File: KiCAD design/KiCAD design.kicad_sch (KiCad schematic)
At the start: 1 part, among them U101 NUCLEO64-F411RE

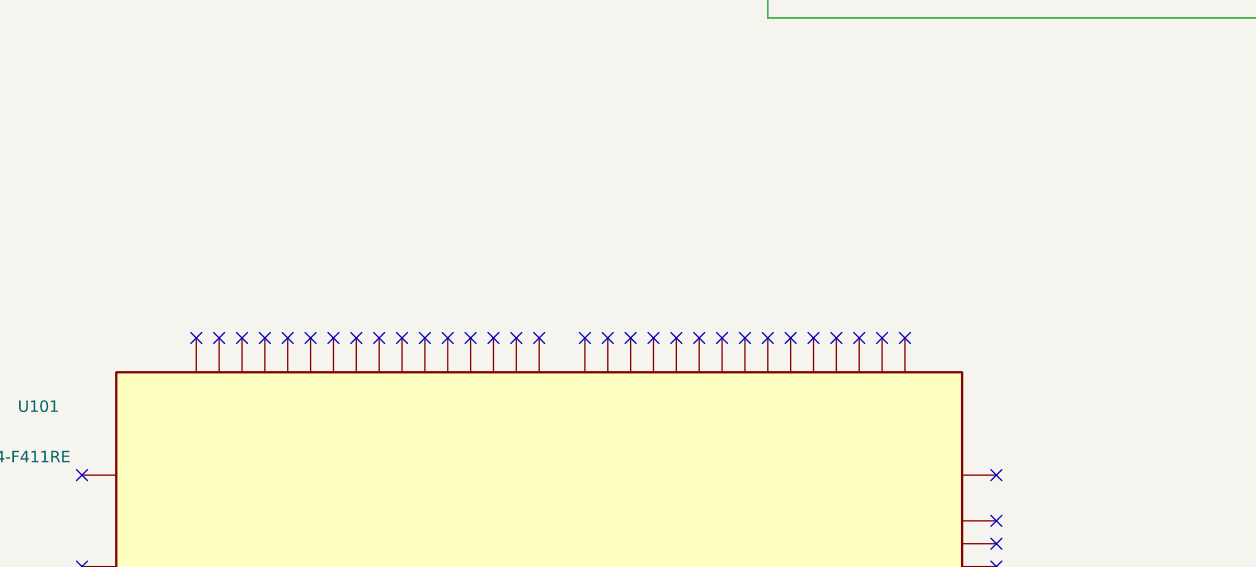
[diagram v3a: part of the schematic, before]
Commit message: comment about nucleo board in main sheet
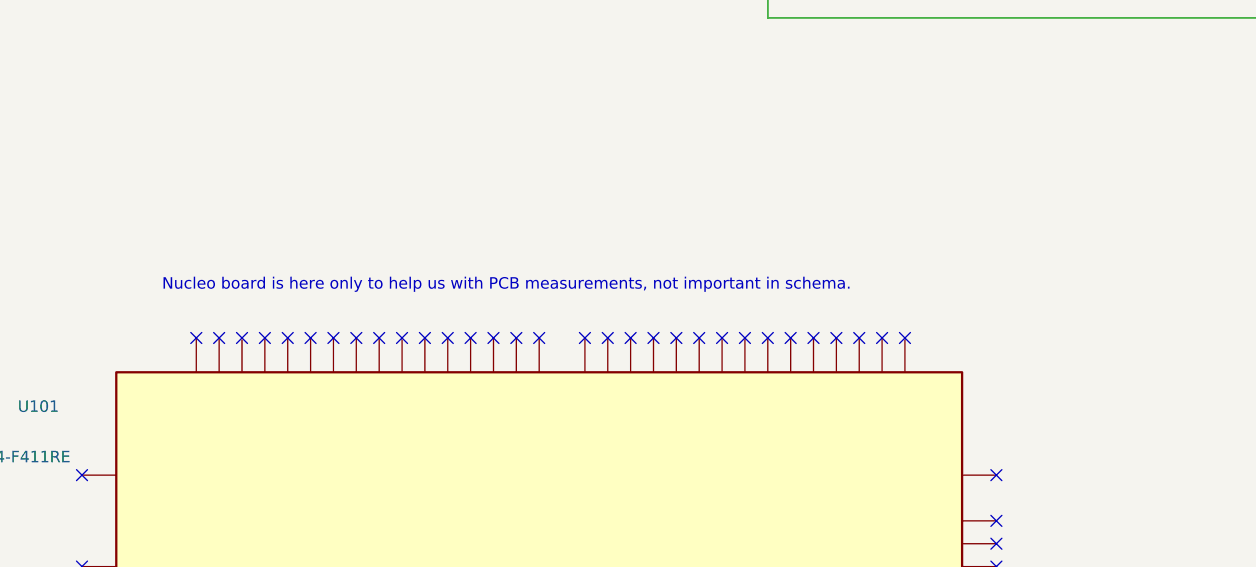
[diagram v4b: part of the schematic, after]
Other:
- note added: "Nucleo board is here only to help us with PCB measurements, not important in schema."
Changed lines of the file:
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@@
     (stroke (width 0) (type default) (color 0 0 0 0))
+  )
+  (text "Nucleo board is here only to help us with PCB measurements, not important in schema."
+    (at 52.07 116.84 0)
+    (effects (font (size 1.27 1.27)) (justify left bottom))
   )
   (symbol (lib_id "MCU_Module:NUCLEO64-F411RE") (at 93.98 149.86 90) (unit 1)

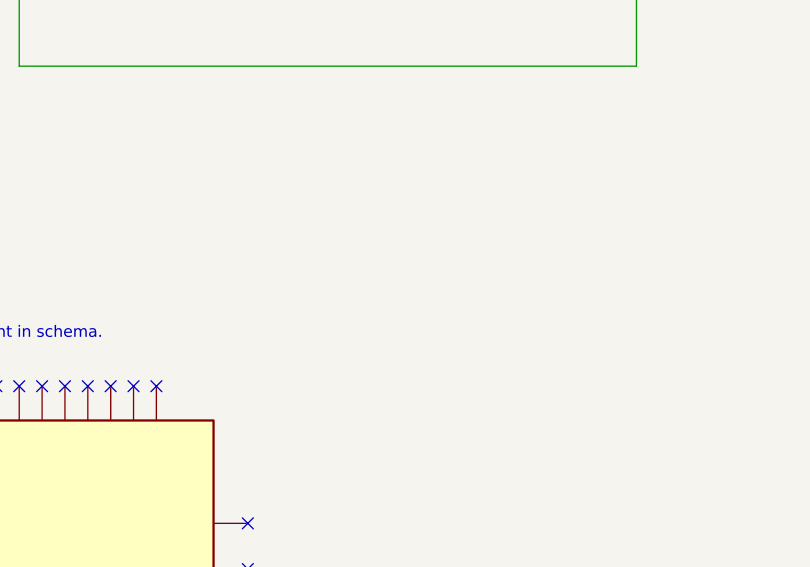
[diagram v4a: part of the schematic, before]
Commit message: change in nucleo pin
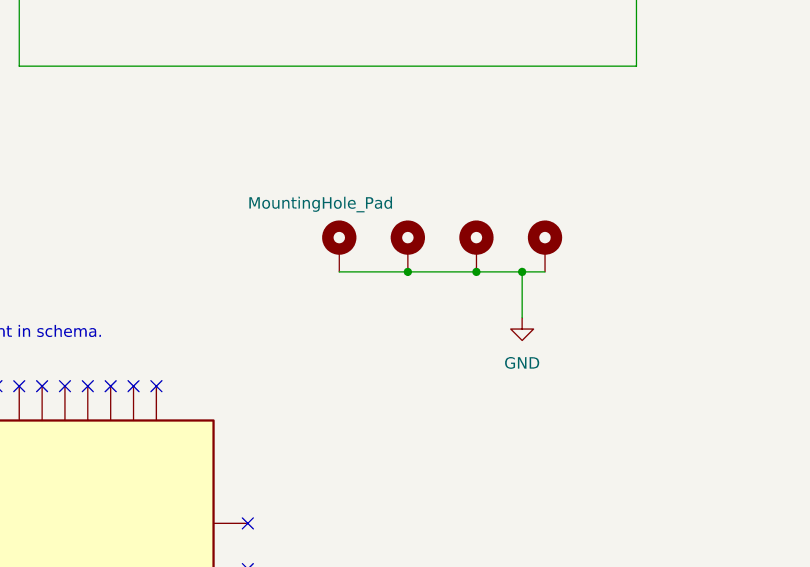
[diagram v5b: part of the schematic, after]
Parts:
- added H101, H102, H103, H104: MountingHole_Pad, MountingHole:MountingHole_3.2mm_M3_Pad_Via, symbol Mechanical:MountingHole_Pad
- U101: footprint Module:ST_Morpho_Connector_144_STLink -> NUCLEO.lib:ST_NUCLEO-F401RE
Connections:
- new net GND: H101.1, H102.1, H103.1, H104.1
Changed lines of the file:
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@@
 (kicad_sch (version 20211123) (generator eeschema)
   (paper "A4")
+  (junction (at 170.18 109.22) (diameter 0) (color 0 0 0 0)
+  )
+  (junction (at 162.56 109.22) (diameter 0) (color 0 0 0 0)
+  )
+  (junction (at 175.26 109.22) (diameter 0) (color 0 0 0 0)
+  )
   (no_connect (at 73.66 121.92))
   (no_connect (at 119.38 121.92))
@@
     (stroke (width 0) (type default) (color 0 0 0 0))
   )
+  (wire (pts (xy 175.26 109.22) (xy 175.26 114.3))
+    (stroke (width 0) (type default) (color 0 0 0 0))
+  )
+  (wire (pts (xy 175.26 109.22) (xy 177.8 109.22))
+    (stroke (width 0) (type default) (color 0 0 0 0))
+  )
+  (wire (pts (xy 154.94 109.22) (xy 162.56 109.22))
+    (stroke (width 0) (type default) (color 0 0 0 0))
+  )
   (wire (pts (xy 73.66 55.88) (xy 127 55.88))
     (stroke (width 0) (type default) (color 0 0 0 0))
@@
     (stroke (width 0) (type default) (color 0 0 0 0))
   )
+  (wire (pts (xy 162.56 109.22) (xy 170.18 109.22))
+    (stroke (width 0) (type default) (color 0 0 0 0))
+  )
   (wire (pts (xy 187.96 68.58) (xy 208.28 68.58))
     (stroke (width 0) (type default) (color 0 0 0 0))
@@
   )
   (wire (pts (xy 73.66 68.58) (xy 119.38 68.58))
+    (stroke (width 0) (type default) (color 0 0 0 0))
+  )
+  (wire (pts (xy 170.18 109.22) (xy 175.26 109.22))
     (stroke (width 0) (type default) (color 0 0 0 0))
   )
@@
     (effects (font (size 1.27 1.27)) (justify left bottom))
   )
+  (symbol (lib_id "Mechanical:MountingHole_Pad") (at 177.8 106.68 0) (unit 1)
+    (in_bom yes) (on_board yes)
+    (property "Reference" "H104" (id 0) (at 167.64 99.06 0)
+      (effects (font (size 1.27 1.27)) (justify left) hide)
+    )
+    (property "Value" "MountingHole_Pad" (id 1) (at 167.64 101.6 0)
+      (effects (font (size 1.27 1.27)) (justify left) hide)
+    )
+    (property "Footprint" "MountingHole:MountingHole_3.2mm_M3_Pad_Via" (id 2) (at 177.8 106.68 0)
+      (effects (font (size 1.27 1.27)) hide)
+    )
+    (property "Datasheet" "~" (id 3) (at 177.8 106.68 0)
+      (effects (font (size 1.27 1.27)) hide)
+    )
+    (pin "1")
+  )
+  (symbol (lib_id "Mechanical:MountingHole_Pad") (at 154.94 106.68 0) (unit 1)
+    (in_bom yes) (on_board yes)
+    (property "Reference" "H101" (id 0) (at 144.78 99.06 0)
+      (effects (font (size 1.27 1.27)) (justify left) hide)
+    )
+    (property "Value" "MountingHole_Pad" (id 1) (at 144.78 101.6 0)
+      (effects (font (size 1.27 1.27)) (justify left))
+    )
+    (property "Footprint" "MountingHole:MountingHole_3.2mm_M3_Pad_Via" (id 2) (at 154.94 106.68 0)
+      (effects (font (size 1.27 1.27)) hide)
+    )
+    (property "Datasheet" "~" (id 3) (at 154.94 106.68 0)
+      (effects (font (size 1.27 1.27)) hide)
+    )
+    (pin "1")
+  )
   (symbol (lib_id "MCU_Module:NUCLEO64-F411RE") (at 93.98 149.86 90) (unit 1)
-    (in_bom no) (on_board yes)
+    (in_bom no) (on_board no)
     (property "Reference" "U101" (id 0) (at 40.64 129.54 90)
       (effects (font (size 1.27 1.27)) (justify left))
@@
       (effects (font (size 1.27 1.27)) (justify left))
     )
-    (property "Footprint" "Module:ST_Morpho_Connector_144_STLink" (id 2) (at 44.45 135.1406 0)
+    (property "Footprint" "NUCLEO.lib:ST_NUCLEO-F401RE" (id 2) (at 44.45 135.1406 0)
       (effects (font (size 1.27 1.27)) (justify left) hide)
     )
@@
     (pin "9")
   )
+  (symbol (lib_id "Mechanical:MountingHole_Pad") (at 162.56 106.68 0) (unit 1)
+    (in_bom yes) (on_board yes)
+    (property "Reference" "H102" (id 0) (at 152.4 99.06 0)
+      (effects (font (size 1.27 1.27)) (justify left) hide)
+    )
+    (property "Value" "MountingHole_Pad" (id 1) (at 152.4 101.6 0)
+      (effects (font (size 1.27 1.27)) (justify left) hide)
+    )
+    (property "Footprint" "MountingHole:MountingHole_3.2mm_M3_Pad_Via" (id 2) (at 162.56 106.68 0)
+      (effects (font (size 1.27 1.27)) hide)
+    )
+    (property "Datasheet" "~" (id 3) (at 162.56 106.68 0)
+      (effects (font (size 1.27 1.27)) hide)
+    )
+    (pin "1")
+  )
+  (symbol (lib_id "Mechanical:MountingHole_Pad") (at 170.18 106.68 0) (unit 1)
+    (in_bom yes) (on_board yes)
+    (property "Reference" "H103" (id 0) (at 160.02 99.06 0)
+      (effects (font (size 1.27 1.27)) (justify left) hide)
+    )
+    (property "Value" "MountingHole_Pad" (id 1) (at 160.02 101.6 0)
+      (effects (font (size 1.27 1.27)) (justify left) hide)
+    )
+    (property "Footprint" "MountingHole:MountingHole_3.2mm_M3_Pad_Via" (id 2) (at 170.18 106.68 0)
+      (effects (font (size 1.27 1.27)) hide)
+    )
+    (property "Datasheet" "~" (id 3) (at 170.18 106.68 0)
+      (effects (font (size 1.27 1.27)) hide)
+    )
+    (pin "1")
+  )
+  (symbol (lib_id "power:GND") (at 175.26 114.3 0) (unit 1)
+    (in_bom yes) (on_board yes) (fields_autoplaced)
+    (property "Reference" "#PWR0115" (id 0) (at 175.26 120.65 0)
+      (effects (font (size 1.27 1.27)) hide)
+    )
+    (property "Value" "GND" (id 1) (at 175.26 119.38 0))
+    (property "Footprint" "" (id 2) (at 175.26 114.3 0)
+      (effects (font (size 1.27 1.27)) hide)
+    )
+    (property "Datasheet" "" (id 3) (at 175.26 114.3 0)
+      (effects (font (size 1.27 1.27)) hide)
+    )
+    (pin "1")
+  )
   (sheet (at 127 25.4) (size 50.8 50.8) (fields_autoplaced)
     (stroke (width 0.1524) (type solid) (color 0 0 0 0))
@@
       (reference "#PWR0114") (unit 1) (value "+3.3V") (footprint "")
     )
+    (path "/90dbed91-b579-480f-b438-dea81ab13820"
+      (reference "#PWR0115") (unit 1) (value "GND") (footprint "")
+    )
     (path "/351b992e-9d0c-41fd-a6c4-f130ac0d9617/ee57b0d0-fc53-46a4-955b-95d218665177"
       (reference "#PWR0201") (unit 1) (value "GND") (footprint "")
@@
       (reference "D403") (unit 1) (value "RED") (footprint "LED_SMD:LED_1206_3216Metric")
     )
+    (path "/359b6eae-d01f-4c07-a65f-0210ec982c6a"
+      (reference "H101") (unit 1) (value "MountingHole_Pad") (footprint "MountingHole:MountingHole_3.2mm_M3_Pad_Via")
+    )
+    (path "/5c3fe545-b369-450e-a10b-a0b610268b87"
+      (reference "H102") (unit 1) (value "MountingHole_Pad") (footprint "MountingHole:MountingHole_3.2mm_M3_Pad_Via")
+    )
+    (path "/882c6f9a-d699-4f16-be4b-a2264fdad17d"
+      (reference "H103") (unit 1) (value "MountingHole_Pad") (footprint "MountingHole:MountingHole_3.2mm_M3_Pad_Via")
+    )
+    (path "/1327a356-e8db-4ffb-895c-129e588e195c"
+      (reference "H104") (unit 1) (value "MountingHole_Pad") (footprint "MountingHole:MountingHole_3.2mm_M3_Pad_Via")
+    )
     (path "/351b992e-9d0c-41fd-a6c4-f130ac0d9617/73cd9a15-3818-472e-a397-2c2e429393a2"
       (reference "J201") (unit 1) (value "Conn_02x19_Odd_Even") (footprint "Connector_PinHeader_2.54mm:PinHeader_2x19_P2.54mm_Vertical")
@@
     )
     (path "/465a2d22-51a7-48d6-b1e0-fc75f581e914/f474059f-5e64-4ec2-8fdf-47fcddcb3229"
-      (reference "SW301") (unit 1) (value "~") (footprint "composants_projet_footprint:1A11-NF5STSE-B")
+      (reference "SW301") (unit 1) (value "~") (footprint "SWITCH lib:E-SWITCH_RR511D1121")
     )
     (path "/84eed88b-177a-45c5-a159-b80e42fc88fa/1effef2d-bafc-46de-9853-a1755d0a3819"
@@
     )
     (path "/53ab80cb-680d-47b5-9042-b10ff93ac434"
-      (reference "U101") (unit 1) (value "NUCLEO64-F411RE") (footprint "Module:ST_Morpho_Connector_144_STLink")
+      (reference "U101") (unit 1) (value "NUCLEO64-F411RE") (footprint "NUCLEO.lib:ST_NUCLEO-F401RE")
     )
     (path "/465a2d22-51a7-48d6-b1e0-fc75f581e914/9480c12b-095c-4fc3-a989-57ee26360abb"

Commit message: exclude mounting holes from BOM
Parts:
- H101, H102, H103, H104: now left out of the parts list
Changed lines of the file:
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@@
   )
   (symbol (lib_id "Mechanical:MountingHole_Pad") (at 177.8 106.68 0) (unit 1)
-    (in_bom yes) (on_board yes)
+    (in_bom no) (on_board yes)
     (property "Reference" "H104" (id 0) (at 167.64 99.06 0)
       (effects (font (size 1.27 1.27)) (justify left) hide)
@@
   )
   (symbol (lib_id "Mechanical:MountingHole_Pad") (at 154.94 106.68 0) (unit 1)
-    (in_bom yes) (on_board yes)
+    (in_bom no) (on_board yes)
     (property "Reference" "H101" (id 0) (at 144.78 99.06 0)
       (effects (font (size 1.27 1.27)) (justify left) hide)
@@
   )
   (symbol (lib_id "Mechanical:MountingHole_Pad") (at 162.56 106.68 0) (unit 1)
-    (in_bom yes) (on_board yes)
+    (in_bom no) (on_board yes)
     (property "Reference" "H102" (id 0) (at 152.4 99.06 0)
       (effects (font (size 1.27 1.27)) (justify left) hide)
@@
   )
   (symbol (lib_id "Mechanical:MountingHole_Pad") (at 170.18 106.68 0) (unit 1)
-    (in_bom yes) (on_board yes)
+    (in_bom no) (on_board yes)
     (property "Reference" "H103" (id 0) (at 160.02 99.06 0)
       (effects (font (size 1.27 1.27)) (justify left) hide)

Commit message: end PCB
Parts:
- H101, H102, H103, H104: now in the parts list
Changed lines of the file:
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@@
   )
   (symbol (lib_id "Mechanical:MountingHole_Pad") (at 177.8 106.68 0) (unit 1)
-    (in_bom no) (on_board yes)
+    (in_bom yes) (on_board yes)
     (property "Reference" "H104" (id 0) (at 167.64 99.06 0)
       (effects (font (size 1.27 1.27)) (justify left) hide)
@@
   )
   (symbol (lib_id "Mechanical:MountingHole_Pad") (at 154.94 106.68 0) (unit 1)
-    (in_bom no) (on_board yes)
+    (in_bom yes) (on_board yes)
     (property "Reference" "H101" (id 0) (at 144.78 99.06 0)
       (effects (font (size 1.27 1.27)) (justify left) hide)
@@
   )
   (symbol (lib_id "Mechanical:MountingHole_Pad") (at 162.56 106.68 0) (unit 1)
-    (in_bom no) (on_board yes)
+    (in_bom yes) (on_board yes)
     (property "Reference" "H102" (id 0) (at 152.4 99.06 0)
       (effects (font (size 1.27 1.27)) (justify left) hide)
@@
   )
   (symbol (lib_id "Mechanical:MountingHole_Pad") (at 170.18 106.68 0) (unit 1)
-    (in_bom no) (on_board yes)
+    (in_bom yes) (on_board yes)
     (property "Reference" "H103" (id 0) (at 160.02 99.06 0)
       (effects (font (size 1.27 1.27)) (justify left) hide)
@@
       (reference "#PWR0403") (unit 1) (value "GND") (footprint "")
     )
+    (path "/351b992e-9d0c-41fd-a6c4-f130ac0d9617/0fa4013b-08dc-4836-ad16-8115d0c7be8b"
+      (reference "#PWR?") (unit 1) (value "+3.3V") (footprint "")
+    )
     (path "/84eed88b-177a-45c5-a159-b80e42fc88fa/e609e455-2f92-47cd-a338-cdee205ff5a8"
       (reference "Bluetooth401") (unit 1) (value "PMOD BLE") (footprint "")
@@
     )
     (path "/351b992e-9d0c-41fd-a6c4-f130ac0d9617/6a8b86f3-5197-4f17-9c95-637d257eaa6f"
-      (reference "J206") (unit 1) (value "JST SENS TOF") (footprint "Connector_PinHeader_2.54mm:PinHeader_1x06_P2.54mm_Vertical")
+      (reference "J206") (unit 1) (value "JST SENS TOF 2") (footprint "Connector_PinHeader_2.54mm:PinHeader_1x06_P2.54mm_Vertical")
     )
     (path "/351b992e-9d0c-41fd-a6c4-f130ac0d9617/77ef5647-5fd0-45a7-8f1c-57b486318a65"
-      (reference "J208") (unit 1) (value "JST SENS TOF") (footprint "Connector_PinHeader_2.54mm:PinHeader_1x06_P2.54mm_Vertical")
+      (reference "J208") (unit 1) (value "JST SENS TOF 1") (footprint "Connector_PinHeader_2.54mm:PinHeader_1x06_P2.54mm_Vertical")
     )
     (path "/351b992e-9d0c-41fd-a6c4-f130ac0d9617/d838b790-e28f-4ba5-a0b5-f1eb535022bc"
